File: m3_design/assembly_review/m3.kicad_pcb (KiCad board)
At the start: 4 copper layers, 46 x 186 mm, 135 parts, among them J1 BAT+ / GND / SW / SW, J2 SWD+DFU 1x6, J3 USB-C 2.0, J9 CAM 5V / GND / RX / TX, U1 STM32H743VIT6, U10 TPS2553DBVR, U11 TPS2121RUXR, U12 TXU0202DCUR, U13 TPS70933DBVR, U2 AP63203WU-7, U3 W25Q128JVSIQ, U4 ICM-45686, U5 MS561101BA03, U6 SAM-M10Q-00B, U7 TPS259570DSGR, U8 AP63200WU-7, U9 TPS259470LRPWR, Y1 25MHz CL8pF

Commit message: M3-ASSY-R2: merge servos, dual fused pyro, arming, pull-pin and buzzer
Adds every remaining hardware function to the single M3 board (46 x 238 mm,
203 positions / 178 fitted parts, 14 sheets):

- Actuator power switch: back-to-back AON6403 from the battery input, gated
  by the U9 logic path so the one external switch still controls everything.
- Single-deploy dual pyro (owner ruling 2026-09-25): two AON7524 channels on
  two independently fused buses (FMEA H-5), separate 4-pos ARM and igniter
  terminals, per-bus arm sense, continuity, cold pull-up (H-1), gate networks
  per MARGIN_PRESCRIPTION P0-1/P0-2, PE3/PE6 sentinels (LED_RED -> PE8).
- Four servos (1 k series, pull-downs, SRV05-4), clamped pull-pin (PC14),
  MLT-8530 buzzer (PA5; pad mapping from the maker spec).
- Backup altimeter fully isolated by ruling: no interface on the board.
- New AON7524 footprint from AOS PO-00047 rev I; U12 LCSC code added.
- tools/export_fab.py (Gerber/drill zip, JLC BOM + CPL); m3_design/
  check_actuators.py (arming break / gate-network contract from PCB nets).

CAD checks only: tools/check.sh DRC 0 / unconnected 0 / parity 0 / ERC 0,
audit OK. No bench, simulation or flight evidence; no R2 firmware yet.

Co-Authored-By: Claude Opus 5.5 <noreply@anthropic.com>
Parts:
- added C120: 2.2uF, rocket:C0603, F.Cu at (13.4, 44.8)
- added C121: 470uF 25V, rocket:CAP-SMD_BD8.0-L8.3-W8.3-LS9.0-FD_H10.5, F.Cu at (26.2, 40.5)
- added C122: 10nF, rocket:C0603, F.Cu at (31.2, 43.3)
- added C126: 220nF 25V X7R, rocket:C0603, F.Cu at (22.6, 65.0)
- added C127: 10nF, rocket:C0603, F.Cu at (22.1, 69.3)
- added C128: 100nF 50V X7R 10%, rocket:C_0603_1608Metric, F.Cu at (18.0, 62.5)
- added C129: 10nF, rocket:C0603, F.Cu at (28.9, 65.9)
- added C138: 220nF 25V X7R, rocket:C0603, F.Cu at (22.6, 49.8)
- added C139: 10nF, rocket:C0603, F.Cu at (22.0, 47.4)
- added C140: 100nF 50V X7R 10%, rocket:C_0603_1608Metric, F.Cu at (18.0, 53.5)
- added C141: 10nF, rocket:C0603, F.Cu at (28.9, 50.0)
- added C150: 22uF, rocket:C0805, F.Cu at (19.2, 71.4)
- added C151: 22uF, rocket:C0805, F.Cu at (19.6, 84.4)
- added C160: 100nF, rocket:C0402, F.Cu at (40.0, 83.8)
- added D120: BAT54A, rocket:SOT-23-3_L2.9-W1.3-P1.90-LS2.4-BR, F.Cu at (26.0, 46.4)
- added D121: SRV05-4, rocket:SOT-23-6_L2.9-W1.6-P0.95-LS2.8-BL, F.Cu at (36.6, 78.0)
- added D122: BAT54S, rocket:SOT-23-3_L2.9-W1.3-P1.90-LS2.4-BR, F.Cu at (43.2, 81.8)
- added D123: 1N5819WS, rocket:SOD-323_L1.8-W1.3-LS2.5-RD, F.Cu at (13.2, 74.0)
- added J120: ARM: RAW / BUS2 / BUS1 / RAW, rocket:M3_DB128V_4P, F.Cu at (36.0, 58.0)
- added J121: E1- / E1+ / E2+ / E2-, rocket:M3_DB128V_4P, F.Cu at (10.0, 58.0)
- added J122: SERVO 3x4, rocket:HDR-TH_12P-P2.54-V-M-R3-C4-S2.54, F.Cu at (23.0, 78.0)
- added J123: PULL-PIN 1x2, rocket:M3_PULLPIN_1x2, F.Cu at (42.0, 74.6)
- added LS120: MLT-8530, rocket:BUZ-SMD_4P-L8.5-W8.5-P8.50-BR, F.Cu at (7.00, 77.0)
- added Q120: AON6403, rocket:PDFN-8_L5.6-W5.2-P1.27-LS6.1-BL, F.Cu at (10.0, 40.5)
- added Q121: AON6403, rocket:PDFN-8_L5.6-W5.2-P1.27-LS6.1-BL, F.Cu at (17.2, 40.5)
- added Q122: AO3400A, rocket:SOT-23-3_L2.9-W1.3-P1.90-LS2.4-BR, F.Cu at (34.2, 39.3)
- added Q123: AO3400A, rocket:SOT-23-3_L2.9-W1.3-P1.90-LS2.4-BR, F.Cu at (13.2, 79.4)
- added Q124: AON7524, rocket:M3_AON7524_DFN3x3A, F.Cu at (18.6, 65.6)
- added Q125: AON7524, rocket:M3_AON7524_DFN3x3A, F.Cu at (18.6, 50.4)
- added R120: 100k, rocket:R0402, F.Cu at (13.5, 36.0)
- added R121: 10k, rocket:R0402, F.Cu at (8.60, 45.6)
- added R122: 100k, rocket:R0402, F.Cu at (31.6, 38.4)
- added R123: 100k, rocket:R0402, F.Cu at (31.6, 39.7)
- added R124: 10k, rocket:R0402, F.Cu at (33.2, 45.0)
- added R125: 4.7k, rocket:R0402, F.Cu at (33.2, 46.3)
- added R126: 220R, rocket:R0805, F.Cu at (24.4, 65.0)
- added R127: 1k, rocket:R0402, F.Cu at (24.1, 68.0)
- added R128: 10k, rocket:R0402, F.Cu at (21.3, 64.9)
- added R129: 10k, rocket:R0402, F.Cu at (17.7, 68.5)
- added R130: 1k, rocket:R0402, F.Cu at (19.6, 68.5)
- added R131: 47k, rocket:R0402, F.Cu at (17.7, 69.7)
- added R132: 10k, rocket:R0402, F.Cu at (29.1, 58.6)
- added R133: 1k, rocket:R0402, F.Cu at (29.1, 64.0)
- added R138: 220R, rocket:R0805, F.Cu at (24.4, 49.8)
- added R139: 1k, rocket:R0402, F.Cu at (24.4, 52.9)
- added R140: 10k, rocket:R0402, F.Cu at (21.3, 49.7)
- added R141: 10k, rocket:R0402, F.Cu at (17.7, 47.4)
- added R142: 1k, rocket:R0402, F.Cu at (19.6, 47.4)
- added R143: 47k, rocket:R0402, F.Cu at (17.7, 46.1)
- added R144: 10k, rocket:R0402, F.Cu at (29.1, 57.4)
- added R145: 1k, rocket:R0402, F.Cu at (29.1, 52.0)
- added R150: 1k 0805, rocket:R0805, F.Cu at (29.6, 81.8)
- added R151: 1k 0805, rocket:R0805, F.Cu at (29.6, 79.3)
- added R152: 1k 0805, rocket:R0805, F.Cu at (29.6, 76.7)
- added R153: 1k 0805, rocket:R0805, F.Cu at (29.6, 74.2)
- added R154: 10k, rocket:R0402, F.Cu at (33.0, 81.8)
- added R155: 10k, rocket:R0402, F.Cu at (33.0, 79.3)
- added R156: 10k, rocket:R0402, F.Cu at (33.0, 76.7)
- added R157: 10k, rocket:R0402, F.Cu at (33.0, 74.2)
- added R160: 1k, rocket:R0402, F.Cu at (40.0, 80.8)
- added R161: 10k, rocket:R0402, F.Cu at (37.9, 83.8)
- added R162: 220R, rocket:R0805, F.Cu at (13.2, 83.4)
- added R163: 10k, rocket:R0402, F.Cu at (15.8, 81.2)
- added TP120: RAW_ACT, rocket:M3_TestPad_1.5, F.Cu at (42.5, 36.4)
- added TP121: ACT_GATE, rocket:M3_TestPad_1.5, F.Cu at (16.8, 35.5)
- added TP122: PYRO1_GATE, rocket:M3_TestPad_1.5, F.Cu at (26.6, 64.0)
- added TP123: PYRO2_GATE, rocket:M3_TestPad_1.5, F.Cu at (26.6, 49.1)
- added TP124: GND, rocket:M3_TestPad_1.5, F.Cu at (20.5, 58.0)
- moved C10 52.0 mm to (30.6, 142.3)
- moved C26 52.0 mm to (20.3, 152.3)
- moved C6 52.0 mm to (12.5, 139.8)
- moved D4 52.0 mm to (13.5, 178.8)
- moved R110 52.0 mm to (18.0, 176.8)
- moved U5 52.0 mm to (39.0, 161.1)
- moved C11 52.0 mm to (34.6, 141.0)
- moved C14 52.0 mm to (12.8, 160.5)
- moved C15 52.0 mm to (12.9, 172.9)
- moved C16 52.0 mm to (31.6, 175.9)
- moved C17 52.0 mm to (33.8, 160.0)
- moved C18 52.0 mm to (26.5, 156.4)
- moved C19 52.0 mm to (12.9, 171.4)
- moved C20 52.0 mm to (28.6, 175.9)
- moved C24 52.0 mm to (39.3, 175.6)
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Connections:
- U1 pad 15: unconnected-(U1-PC0-Pad15) -> PYRO1_CONT
- U1 pad 16: unconnected-(U1-PC1-Pad16) -> PYRO2_CONT
- U1 pad 2: LED_RED -> unconnected-(U1-PE3-Pad2)
- U1 pad 22: unconnected-(U1-PA0-Pad22) -> SERVO1_MCU
- U1 pad 23: unconnected-(U1-PA1-Pad23) -> SERVO2_MCU
- U1 pad 24: unconnected-(U1-PA2-Pad24) -> SERVO3_MCU
- U1 pad 25: unconnected-(U1-PA3-Pad25) -> SERVO4_MCU
- U1 pad 29: unconnected-(U1-PA5-Pad29) -> BUZZ_DRV
- U1 pad 3: unconnected-(U1-PE4-Pad3) -> PYRO1_GATE_N
- U1 pad 32: unconnected-(U1-PC4-Pad32) -> ARM2_SENSE
- U1 pad 33: unconnected-(U1-PC5-Pad33) -> ARM1_SENSE
- U1 pad 34: unconnected-(U1-PB0-Pad34) -> RAW_ACT_SENSE
- U1 pad 38: unconnected-(U1-PE8-Pad38) -> LED_RED
- U1 pad 4: unconnected-(U1-PE5-Pad4) -> PYRO2_GATE_N
- U1 pad 8: unconnected-(U1-PC14-Pad8) -> PULLPIN
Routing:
- net RAW_ACT_SENSE: track 0.00 -> 137.3 mm, vias 0 -> 9
- net ARM2_SENSE: track 0.00 -> 137.1 mm, vias 0 -> 5
- net ARM1_SENSE: track 0.00 -> 124.4 mm, vias 0 -> 5
- net PYRO1_GATE_N: track 0.00 -> 120.5 mm, vias 0 -> 5
- net PYRO2_GATE_N: track 0.00 -> 118.9 mm, vias 0 -> 4
- net PYRO2_CONT: track 0.00 -> 117.5 mm, vias 0 -> 3
- net 3V3: track 225.9 -> 342.5 mm, vias 26 -> 36
- net SERVO4_MCU: track 0.00 -> 104.6 mm, vias 0 -> 5
- net PYRO1_CONT: track 0.00 -> 100.9 mm, vias 0 -> 5
- net SERVO3_MCU: track 0.00 -> 98.1 mm, vias 0 -> 4
- net SERVO2_MCU: track 0.00 -> 97.4 mm, vias 0 -> 6
- net PULLPIN: track 0.00 -> 96.4 mm, vias 0 -> 2
- net SERVO1_MCU: track 0.00 -> 96.1 mm, vias 0 -> 7
- net BUZZ_DRV: track 0.00 -> 80.8 mm, vias 0 -> 2
- net RAW_PROTECTED: track 68.2 -> 126.1 mm, vias 4 -> 5
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- added copper zone on F.Cu, net ACT_FET_S
- added copper zone on F.Cu, net BAT_IN
- added copper zone on In2.Cu, net BAT_IN
- added copper zone on F.Cu, net RAW_ACT
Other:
- board size 46 x 186 mm -> 46 x 238 mm
- board text added: "-"
- board text added: "1"
- board text added: "15A FUSE IN BATTERY LEAD"
- board text added: "2"
- board text added: "2S INPUT / M3-ASSY-R2"
- board text added: "3"
- board text added: "4"
- board text added: "5A FAST FUSES, PLUG IN LAST"
- board text added: "ARM"
- board text added: "ARM PLUG: 4-F1-3 / 1-F2-2"
- board text added: "BUS1"
- board text added: "BUS2"
- board text added: "E1+"
- board text added: "E1-"
- board text added: "E2+"
- board text added: "E2-"
- board text added: "IGNITERS"
- board text added: "M3-ASSY-R2 - DATA"
- board text added: "PULL"
- board text added: "RAW"
- board text added: "S"
- board text added: "SERVO"
- board text removed: "2S INPUT / M3-ASSY-R1"
- board text removed: "CAMERA POWER - ASSY-R1"
- board text removed: "M3-ASSY-R1 - DATA"

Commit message: Limit a shorted igniter to ~4 A: R134/R135 2 ohm pulse resistors, 10k cold pull-ups
Simulation of R2 as merged showed that firing into a shorted igniter pulled
BAT_IN below 5 V for 4-20 ms until the 5 A arming fuse melted (MCU reset,
channel 2 lost) and overstressed the AON7524 at a fresh pack.

- R134/R135 Bourns CRM2512-FX-2R00ELF (C3013496) in series between each fused
  bus and the igniter terminal (new nets PYRO1_IGN/PYRO2_IGN); arm sense stays
  on the plug side. Placed in line on the bus straps; TP124 moved, four
  references moved to free silkscreen.
- R131/R143 cold pull-ups 47k -> 10k for plug-out self-test margin.
- check_actuators.py contract updated (+ negative cases verified by hand).
- sim_r2 models the fix as drawn: all current-design cases pass; the merged
  design is kept as OLD-FAIL comparison rows.
- Firmware requirements recorded: 20 ms fire pulse, resume after reset.

DRC 0 / unconnected 0 / parity 0 / ERC 0, audit OK; diagnostics 173, firmware
112, quality_audit 12 tests pass.

Co-Authored-By: Claude Opus 5.5 (1M context) <noreply@anthropic.com>
Claude-Session: https://claude.ai/code/session_01DdkfTxR7SVyv9xZNmPk9vB
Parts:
- added R134: 2R 1% 2W pulse, rocket:R2512, F.Cu at (23.8, 60.5)
- added R135: 2R 1% 2W pulse, rocket:R2512, F.Cu at (23.8, 56.1)
- R131, R143: value 47k -> 10k
- moved TP124 2.60 mm to (17.9, 58.0)
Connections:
- J121 pad 2: PYRO1_BUS -> PYRO1_IGN
- J121 pad 3: PYRO2_BUS -> PYRO2_IGN
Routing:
- net PYRO2_BUS: track 27.9 -> 11.1 mm
- net PYRO1_BUS: track 27.9 -> 11.1 mm
- net PYRO2_IGN: track 0.00 -> 10.8 mm
- net PYRO1_IGN: track 0.00 -> 10.8 mm

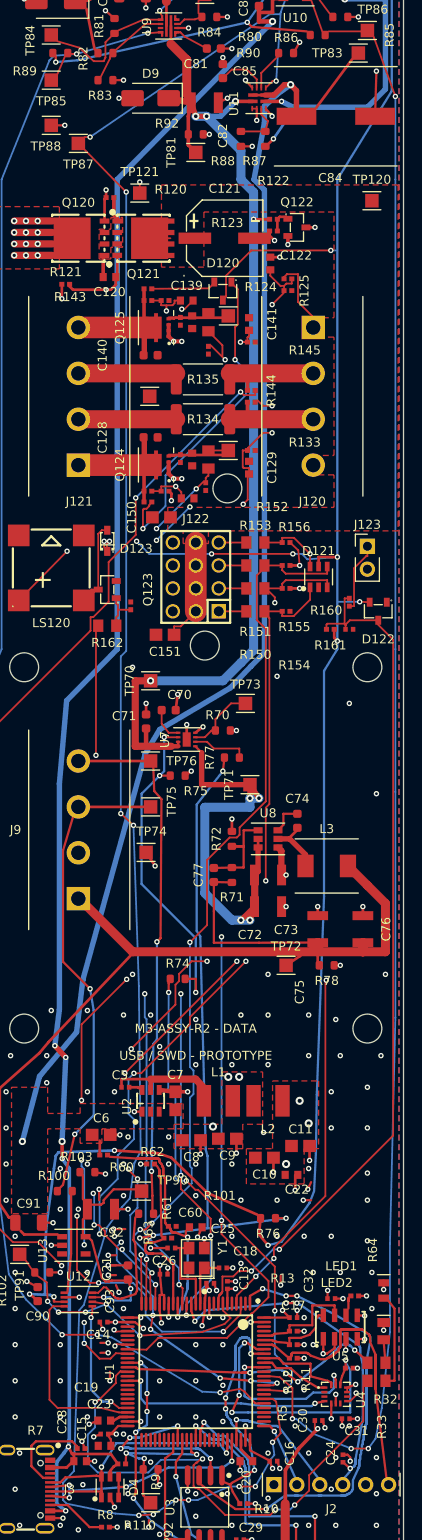
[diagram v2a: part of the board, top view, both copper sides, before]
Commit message: R2 part-by-part datasheet verification; fix every issue found
All 99 BOM lines / 205 positions checked against manufacturer datasheets
(pinout, land pattern, polarity, part number, 3D orientation); record in
docs/R2_VERIFICATION.md.

Fixes:
- R134/R135: Bourns CRM2512 recommended land (2.45 x 3.7 mm pads, 7.6 mm),
  moved to keep clearance; generic 2512 land had ~45 % of the pad area.
- BOOT0 rerouted out from between the MS5611 pads (TE: do not route
  between pads); 0/45/90 segments instead of 0.1 mm staircases.
- C84 polarity mark on the top side; U12 pin-1 mark.
- AON7524 3D model rotated 180 deg; L1/L2 model height 3.0 mm.
- R84 C705743, R9 C25915, R86 80.6k 0.1% C861568 (80k not orderable);
  every BOM line now has an LCSC code.
- sim_r2: fire with all four servos stalled (FMEA V-15) passes.
- FMEA H-1..H-10 status, redundancy table, firmware requirements,
  README / STATUS / AGENTS updated for R2.

DRC 0 / unconnected 0 / parity 0 / ERC 0, audit OK, actuator contract OK;
diagnostics 173, firmware 112, quality_audit 12 tests pass; sim 135 PASS.

Co-Authored-By: Claude Opus 5.5 (1M context) <noreply@anthropic.com>
Claude-Session: https://claude.ai/code/session_01DdkfTxR7SVyv9xZNmPk9vB
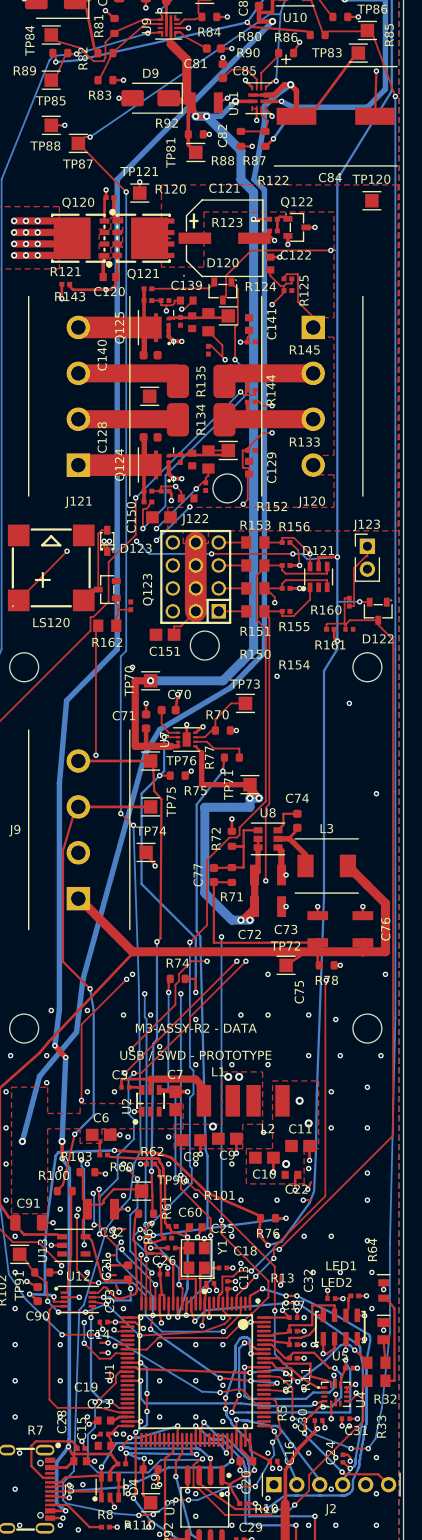
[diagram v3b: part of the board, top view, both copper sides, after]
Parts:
- R86: value 80k 0.1% -> 80.6k 0.1%
- moved R135 0.30 mm to (23.6, 56.4)
- moved R134 0.21 mm to (23.6, 60.6)
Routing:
- net BOOT0: track 30.3 -> 31.3 mm, vias 0 -> 4

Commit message: Make R2 orderable: stocked drop-ins, JLC placement corrections, ordering guide
- Stock (JLC assembly API): U8 AP63200 -> AP63300WU-7 (same TSOT26 pinout,
  VFB, fsw), L3 -> SRP5030T-6R8M (same body/land, AP63300 Table 1), C77
  100p -> 47p (Table 1), C84 25SVPF330M -> 35SVPK330M (same OS-CON F12).
  Every BOM line now has JLC stock for 5 boards except U6 SAM-M10Q
  (consign / Global Sourcing; DigiKey has stock).
- tools/jlc_orient.py matches each footprint pad-by-pad to the LCSC/EasyEDA
  footprint of its LCSC code; export_fab.py applies the rotation/offset.
  Without it U7, U8, U10, U11, U12, U13, D121 and LED2 would be rotated.
- tools/jlc_stock.py: repeatable stock check; fab/stock_check.json.
- JLC_Assembly field: U6 consign note, J2/J123 hand-cut from one 1x40 strip.
- docs/ORDERING.md: PCB options, PCBA, preview checklist, off-board parts.

DRC 0 / unconnected 0 / parity 0 / ERC 0, audit OK; contract OK;
tests 173/112/12 pass; sim 135 PASS.

Co-Authored-By: Claude Opus 5.5 (1M context) <noreply@anthropic.com>
Claude-Session: https://claude.ai/code/session_01DdkfTxR7SVyv9xZNmPk9vB
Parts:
- C77: value 100pF 50V C0G 5% -> 47pF 50V C0G 5%
- C84: value 330uF 25V -> 330uF 35V
- L3: value 10uH -> 6.8uH
- U8: value AP63200WU-7 -> AP63300WU-7
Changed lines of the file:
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@@
 			)
 		)
+		(property "JLC_Assembly" "Consign or JLC Global Sourcing: SAM-M10Q-00B from DigiKey (JLC stock 0 on 2026-09-27)"
+			(at 0 0 0)
+			(layer "F.SilkS")
+			(hide yes)
+			(effects
+				(font
+					(size 1.27 1.27)
+					(thickness 0.15)
+				)
+			)
+		)
 		(attr smd)
 		(duplicate_pad_numbers_are_jumpers no)
@@
 			)
 		)
-		(property "Value" "100pF 50V C0G 5%"
+		(property "Value" "47pF 50V C0G 5%"
 			(at 0 1.43 90)
 			(layer "F.Fab")
@@
 			)
 		)
-		(property "LCSC" "C14858"
+		(property "LCSC" "C1671"
 			(at 0 0 0)
 			(layer "F.SilkS")
@@
 			)
 		)
-		(property "LCSC Part" "C14858"
+		(property "LCSC Part" "C1671"
 			(at 0 0 0)
 			(layer "F.SilkS")
@@
 			)
 		)
-		(property "Manufacturer Part" "CL10C101JB8NNNC"
+		(property "Manufacturer Part" "CL10C470JB8NNNC"
 			(at 0 0 0)
 			(layer "F.SilkS")
@@
 			)
 		)
+		(property "JLC_Assembly" "Hand: cut 1x6 from the 1x40 strip C2337 (one strip covers J2 and J123)"
+			(at 0 0 0)
+			(layer "F.SilkS")
+			(hide yes)
+			(effects
+				(font
+					(size 1.27 1.27)
+					(thickness 0.15)
+				)
+			)
+		)
 		(attr through_hole)
 		(duplicate_pad_numbers_are_jumpers no)
@@
 			)
 		)
+		(property "JLC_Assembly" "Hand: cut 1x2 from the same 1x40 strip C2337 as J2"
+			(at 0 0 0)
+			(layer "F.SilkS")
+			(hide yes)
+			(effects
+				(font
+					(size 1.27 1.27)
+					(thickness 0.15)
+				)
+			)
+		)
 		(sheetname "14 | Launch pull-pin and buzzer")
 		(sheetfile "pullpin_buzzer.kicad_sch")
@@
 			)
 		)
-		(property "Value" "10uH"
+		(property "Value" "6.8uH"
 			(at 0 4.1 0)
 			(layer "F.Fab")
@@
 			)
 		)
-		(property "LCSC" "C3223923"
+		(property "LCSC" "C1329837"
 			(at 0 0 0)
 			(layer "F.SilkS")
@@
 			)
 		)
-		(property "LCSC Part" "C3223923"
+		(property "LCSC Part" "C1329837"
 			(at 0 0 0)
 			(layer "F.SilkS")
@@
 			)
 		)
-		(property "Manufacturer Part" "SRP5030TA-100M"
+		(property "Manufacturer Part" "SRP5030T-6R8M"
 			(at 0 0 0)
 			(layer "F.SilkS")
@@
 			)
 		)
-		(property "Value" "330uF 25V"
+		(property "Value" "330uF 35V"
 			(at 0 6.6 0)
 			(layer "F.Fab")
@@
 			)
 		)
-		(property "LCSC" "C178367"
+		(property "LCSC" "C178373"
 			(at 0 0 0)
 			(layer "F.SilkS")
@@
 			)
 		)
-		(property "LCSC Part" "C178367"
+		(property "LCSC Part" "C178373"
 			(at 0 0 0)
 			(layer "F.SilkS")
@@
 			)
 		)
+		(property "Manufacturer" "Panasonic"
+			(at 0 0 0)
+			(layer "F.SilkS")
+			(hide yes)
+			(effects
+				(font
+					(size 1.27 1.27)
+				)
+			)
+		)
+		(property "Manufacturer Part" "35SVPK330M"
+			(at 0 0 0)
+			(layer "F.SilkS")
+			(hide yes)
+			(effects
+				(font
+					(size 1.27 1.27)
+				)
+			)
+		)
 		(attr smd)
 		(duplicate_pad_numbers_are_jumpers no)
@@
 			)
 		)
-		(property "Value" "AP63200WU-7"
+		(property "Value" "AP63300WU-7"
 			(at 0 2.85 0)
 			(layer "F.Fab")
@@
 			)
 		)
-		(property "LCSC" "C2071868"
+		(property "LCSC" "C2158012"
+			(at 0 0 0)
+			(layer "F.SilkS")
+			(hide yes)
+			(effects
+				(font
+					(size 1.27 1.27)
+					(thickness 0.15)
+				)
+			)
+		)
+		(property "LCSC Part" "C2158012"
+			(at 0 0 0)
+			(layer "F.SilkS")
+			(hide yes)
+			(effects
+				(font
+					(size 1.27 1.27)
+					(thickness 0.15)
+				)
+			)
+		)
+		(property "Manufacturer" "Diodes Incorporated"
 			(at 0 0 0)
 			(layer "F.SilkS")
@@
 			)
 		)
-		(property "LCSC Part" "C2071868"
+		(property "Manufacturer Part" "AP63300WU-7"
 			(at 0 0 0)
 			(layer "F.SilkS")
